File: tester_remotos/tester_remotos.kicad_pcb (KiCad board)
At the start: 2 copper layers, 15 parts, among them J1 USB_B, Q1 BC548, U1 4093, U2 VS1838B

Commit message: Módulo "probador de control remoto" terminado.
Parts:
- added J2: CONN_01X01, Wire_Pads:SolderWirePad_single_1mmDrill, F.Cu at (41.3, 31.1)
- added J3: CONN_01X01, Wire_Pads:SolderWirePad_single_1mmDrill, F.Cu at (34.9, 31.1)
- C4: moved to B.Cu
- U2: footprint Pin_Headers:Pin_Header_Straight_1x03 -> opto:VS1838B
- moved U2 78.6 mm to (79.4, 45.7), turned to 180 degrees
- moved R2 73.2 mm to (67.9, 31.8), turned to 180 degrees
- moved RV1 64.3 mm to (50.2, 28.6), turned to 90 degrees
- moved BZ1 51.1 mm to (76.2, 30.5), turned to 90 degrees
- moved Q1 39.8 mm to (67.9, 26.7), turned to 180 degrees
- moved C4 38.5 mm to (60.3, 26.7)
- moved R3 37.6 mm to (67.3, 52.7), turned to 180 degrees
- moved D1 35.0 mm to (76.2, 50.8), turned to 180 degrees
- moved D2 26.4 mm to (66.7, 47.6), turned to 180 degrees
- moved C2 22.5 mm to (73.0, 41.9), turned to 90 degrees
- moved C3 20.5 mm to (39.4, 26.7), turned to 180 degrees
- moved J1 5.41 mm to (41.9, 41.9)
- moved R1 4.46 mm to (53.3, 52.1), turned to 180 degrees
- moved C1 2.62 mm to (40.0, 52.1)
- moved U1 0.32 mm to (50.2, 44.5)
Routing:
- net GND: track 0.00 -> 164.2 mm
- net +5V: track 0.00 -> 71.5 mm
- net Net-(C3-Pad1): track 0.00 -> 42.3 mm
- net Net-(U1-Pad1): track 0.00 -> 38.9 mm
- net Net-(C2-Pad1): track 0.00 -> 30.3 mm, vias 0 -> 4
- net Net-(RV1-Pad1): track 0.00 -> 28.4 mm
- net Net-(D1-Pad2): track 0.00 -> 21.4 mm, vias 0 -> 2
- net Net-(R1-Pad2): track 0.00 -> 16.3 mm
- net Net-(BZ1-Pad2): track 0.00 -> 8.26 mm
- net Net-(R2-Pad2): track 0.00 -> 5.08 mm
- net Net-(Q1-Pad2): track 0.00 -> 4.34 mm
- net Net-(D2-Pad2): track 0.00 -> 3.70 mm
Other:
- board outline added: 50.2 x 33.7 mm
- net class Default: clearance 0.2 -> 0.254; trace_width 0.25 -> 0.508; via_dia 0.6 -> 1.3; via_drill 0.4 -> 0.7
- rule trace_clearance: 0.2 -> 0.254

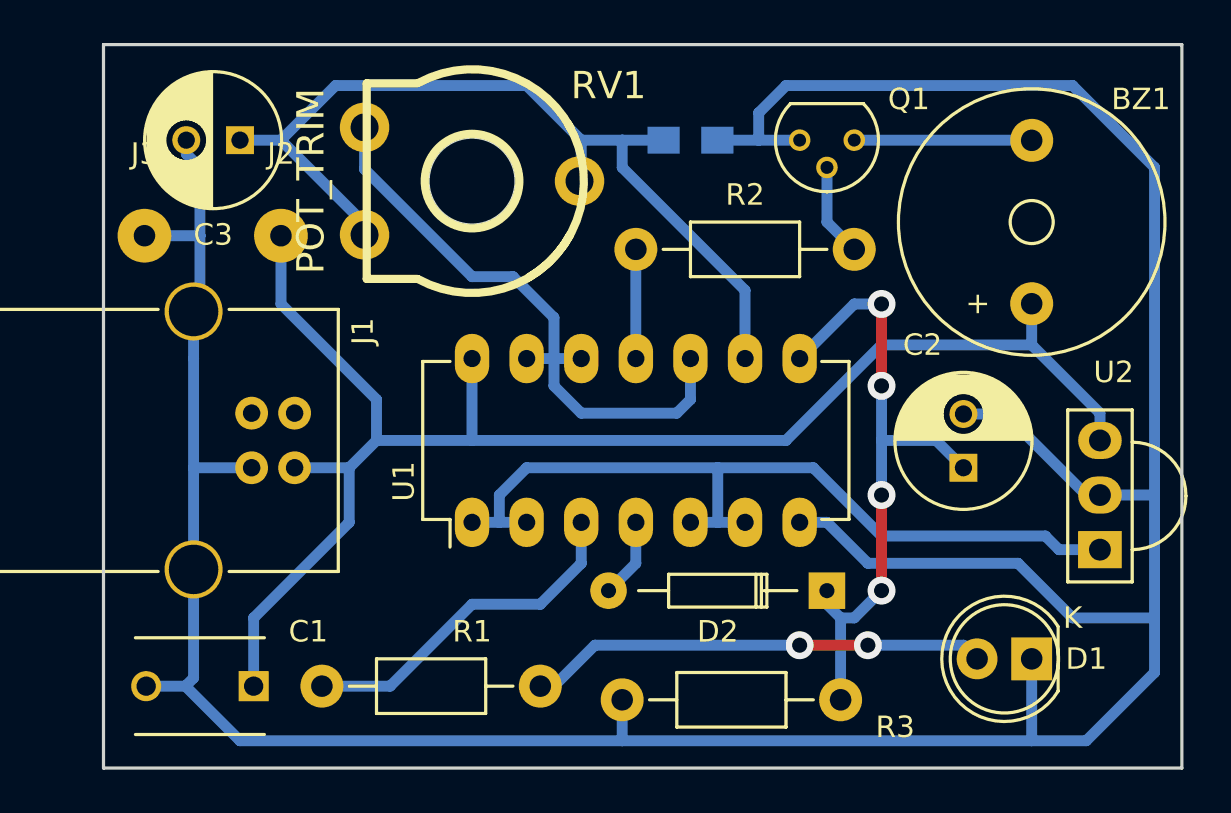
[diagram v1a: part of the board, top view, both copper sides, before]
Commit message: Modificado de pads de varios footprints. Correción de algunos textos en esquemático.
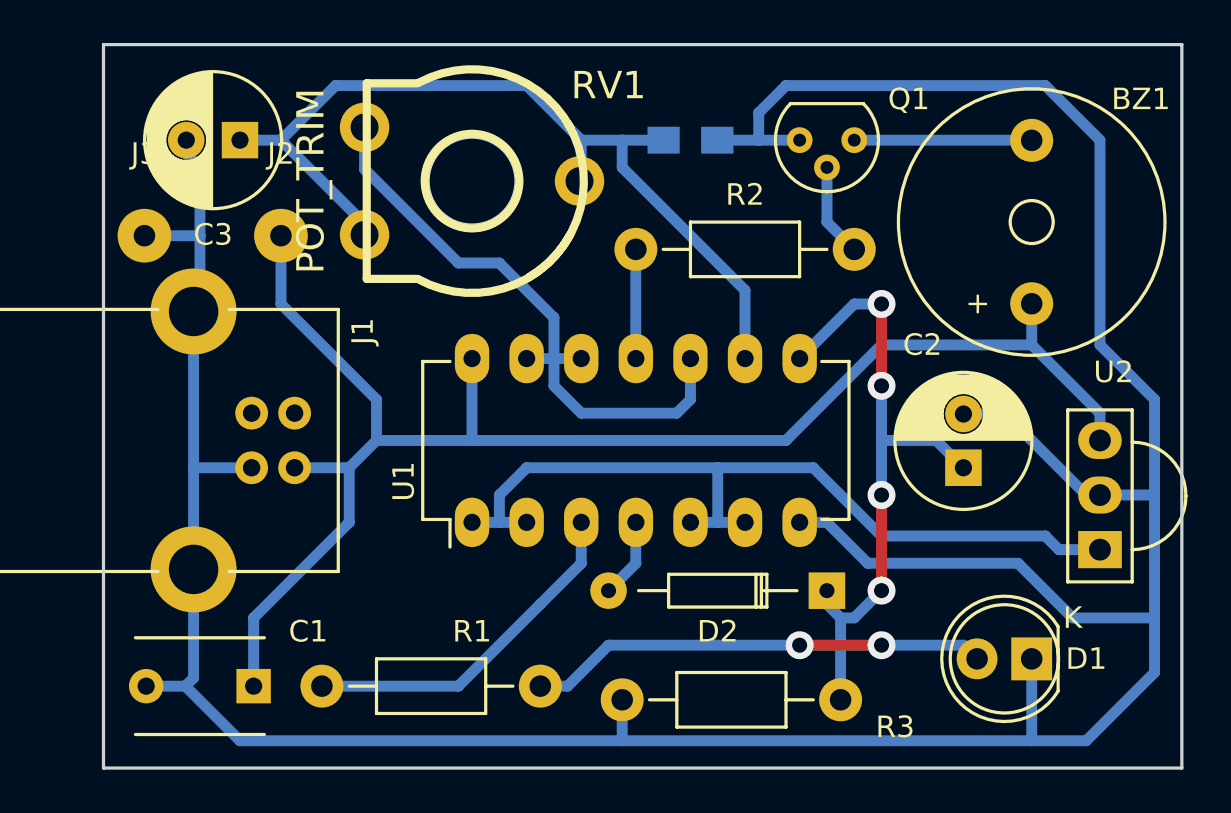
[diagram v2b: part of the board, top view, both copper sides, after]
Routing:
- net GND: track 164.2 -> 163.5 mm

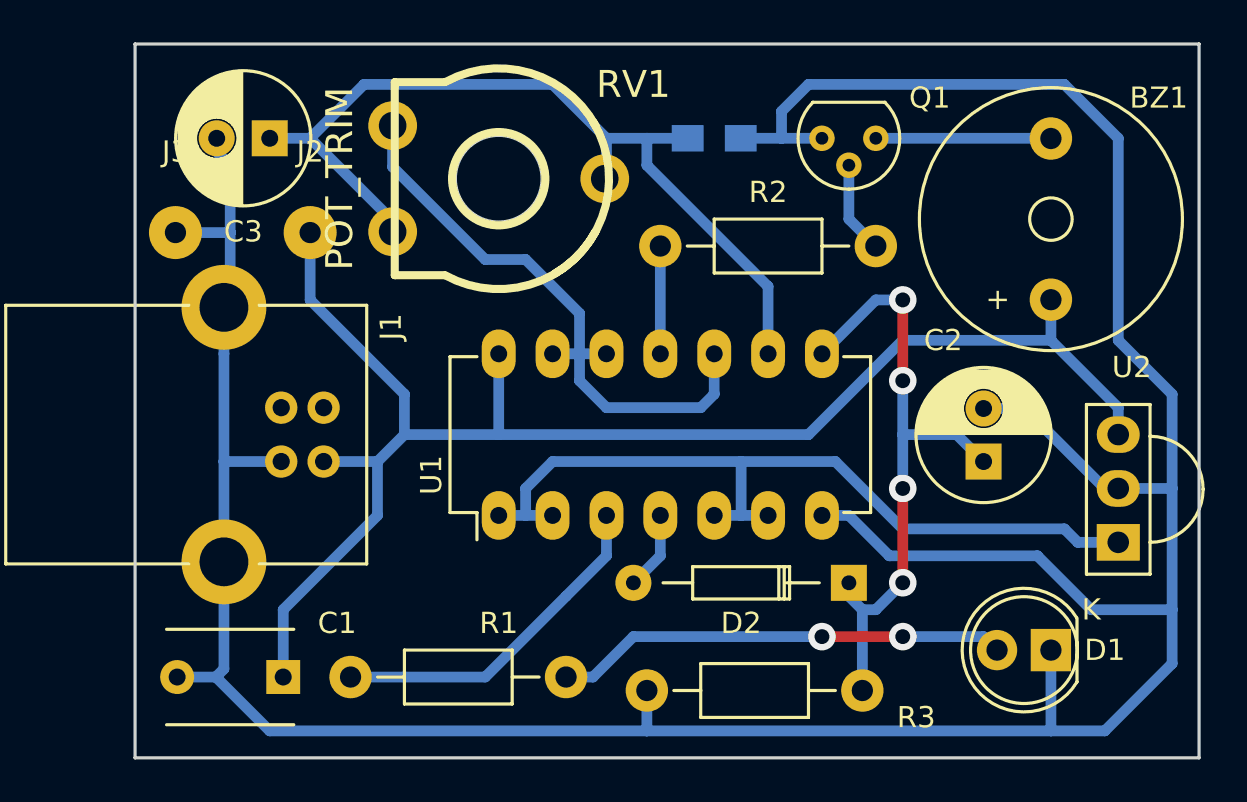
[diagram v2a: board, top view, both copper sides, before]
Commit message: Mejoro clearance a 0,5 mm y actualizo a KiCad 5.1.
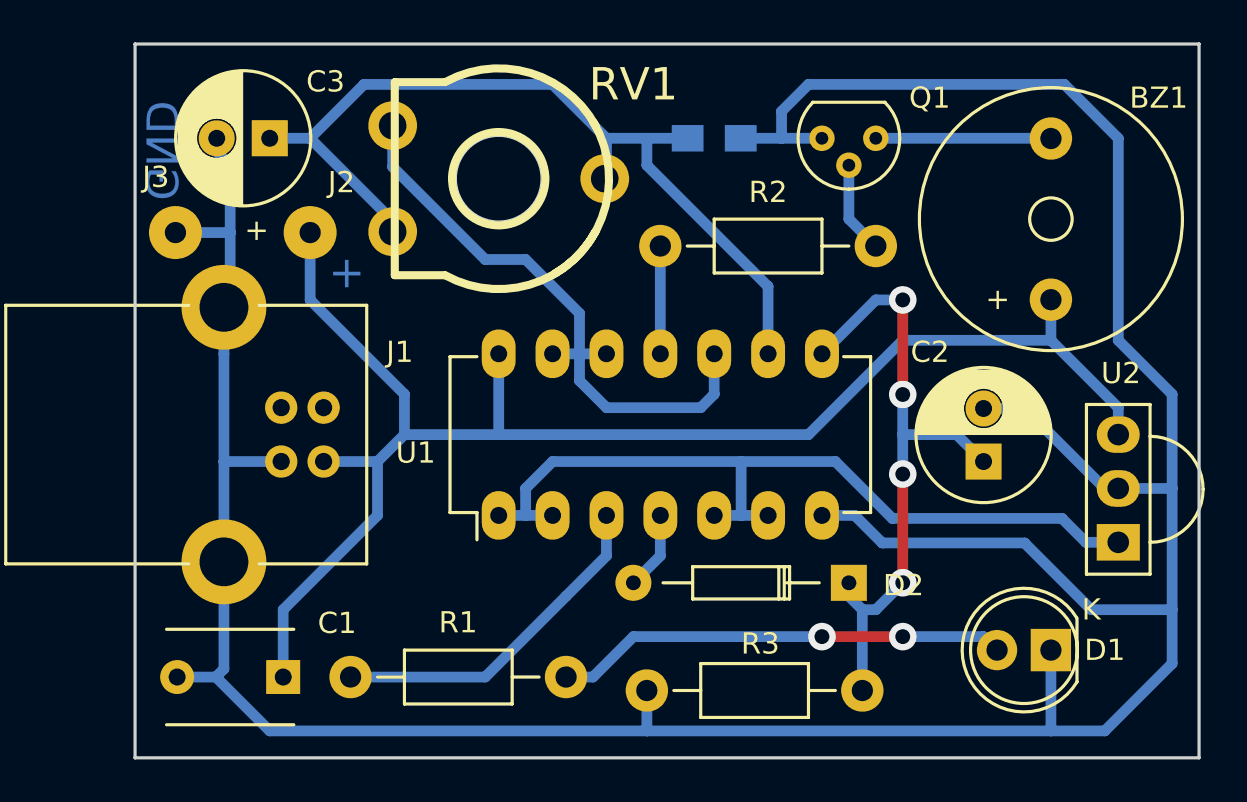
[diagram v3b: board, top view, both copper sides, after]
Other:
- net class Default: clearance 0.254 -> 0.5
- rule trace_clearance: 0.254 -> 0.5
- board text added: "+"
- board text added: "GND"
